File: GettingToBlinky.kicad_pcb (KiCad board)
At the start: 2 copper layers, 33 x 30.5 mm, 7 parts, among them U1 7555

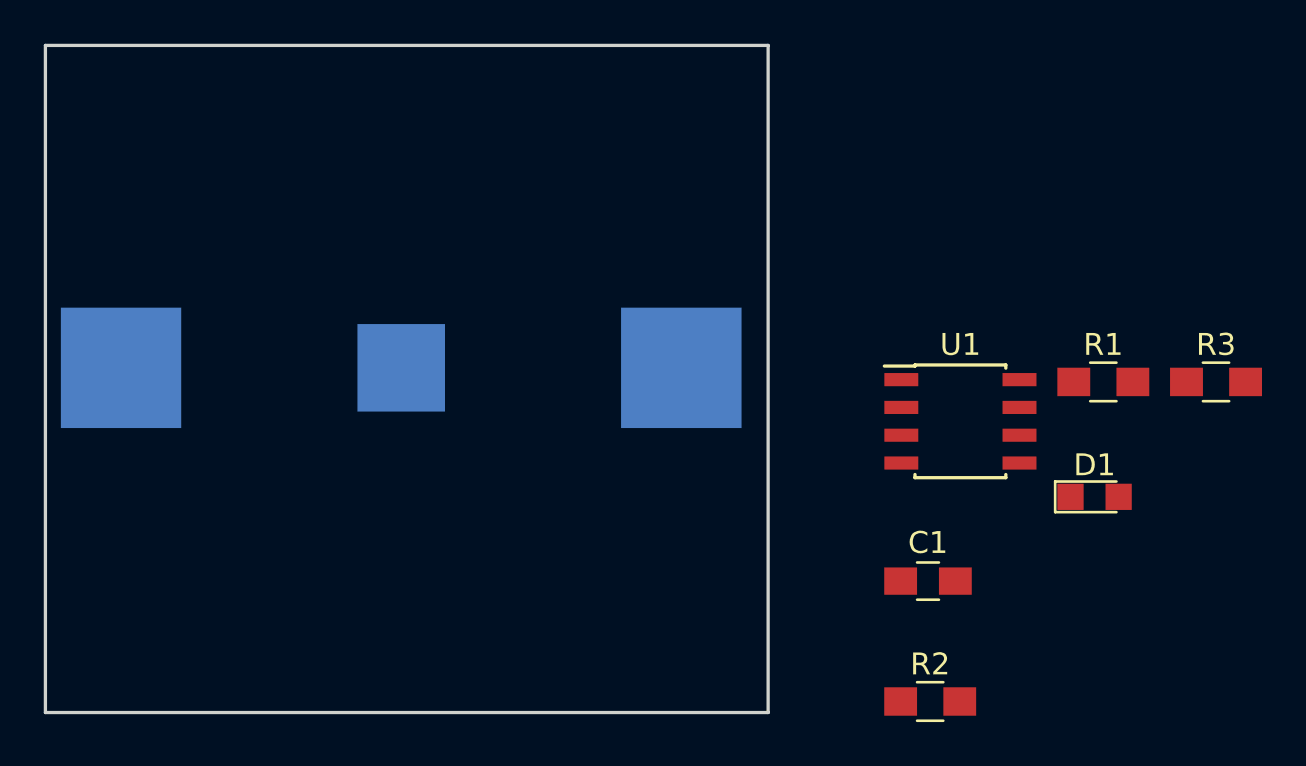
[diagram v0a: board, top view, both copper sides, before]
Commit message: finished connecting all the components with tracks and filled in the copper
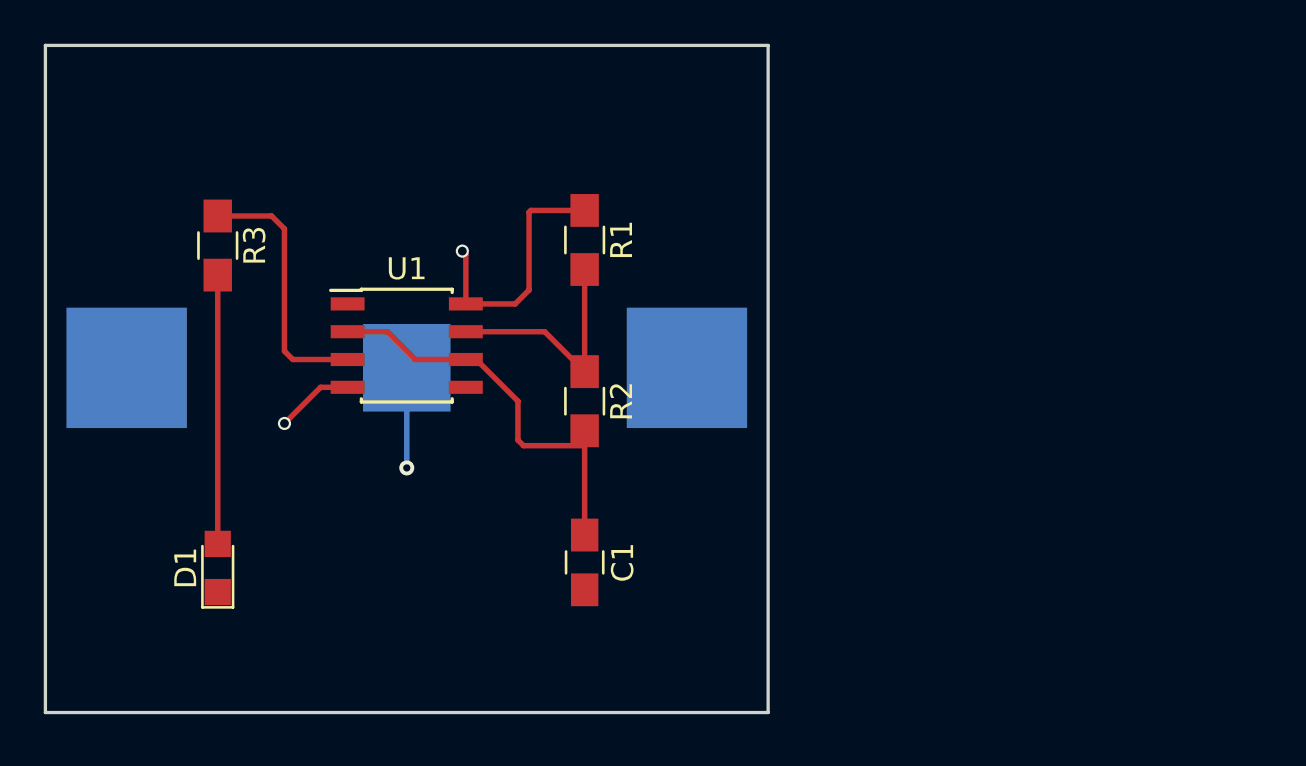
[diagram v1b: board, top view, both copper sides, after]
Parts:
- moved R3 46.0 mm to (96.8, 77.7), turned to 270 degrees
- moved D1 40.2 mm to (96.8, 92.5), turned to 90 degrees
- moved U1 25.5 mm to (105.4, 82.3)
- moved R1 24.6 mm to (113.5, 77.5), turned to 270 degrees
- moved R2 20.9 mm to (113.5, 84.8), turned to 270 degrees
- moved C1 15.7 mm to (113.5, 92.2), turned to 270 degrees
- moved BT1 0.25 mm to (105.4, 83.3)
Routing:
- net Net-(C1-Pad1): track 0.00 -> 19.5 mm
- net /VDD: track 0.00 -> 15.6 mm, vias 0 -> 2
- net Net-(D1-Pad2): track 0.00 -> 12.3 mm
- net Net-(R3-Pad1): track 0.00 -> 11.9 mm
- net Net-(R1-Pad2): track 0.00 -> 10.8 mm
- net GND: track 0.00 -> 4.57 mm, vias 0 -> 1
- added copper zone on B.Cu, net /VDD
- added copper zone on F.Cu, net GND
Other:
- net class Default: clearance 0.2 -> 0.254; trace_width 0.25 -> 0.254; via_dia 0.6 -> 0.6858; via_drill 0.4 -> 0.3302
- rule trace_clearance: 0.2 -> 0.254
- rule trace_min: 0.2 -> 0.1524
- rule via_min_drill: 0.3 -> 0.3302
- rule via_min_size: 0.4 -> 0.6858

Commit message: Updated silk layer to have text I wanted. Lastly ran the design rule checker to make sure all tracks are connected and design rule constraints are passing
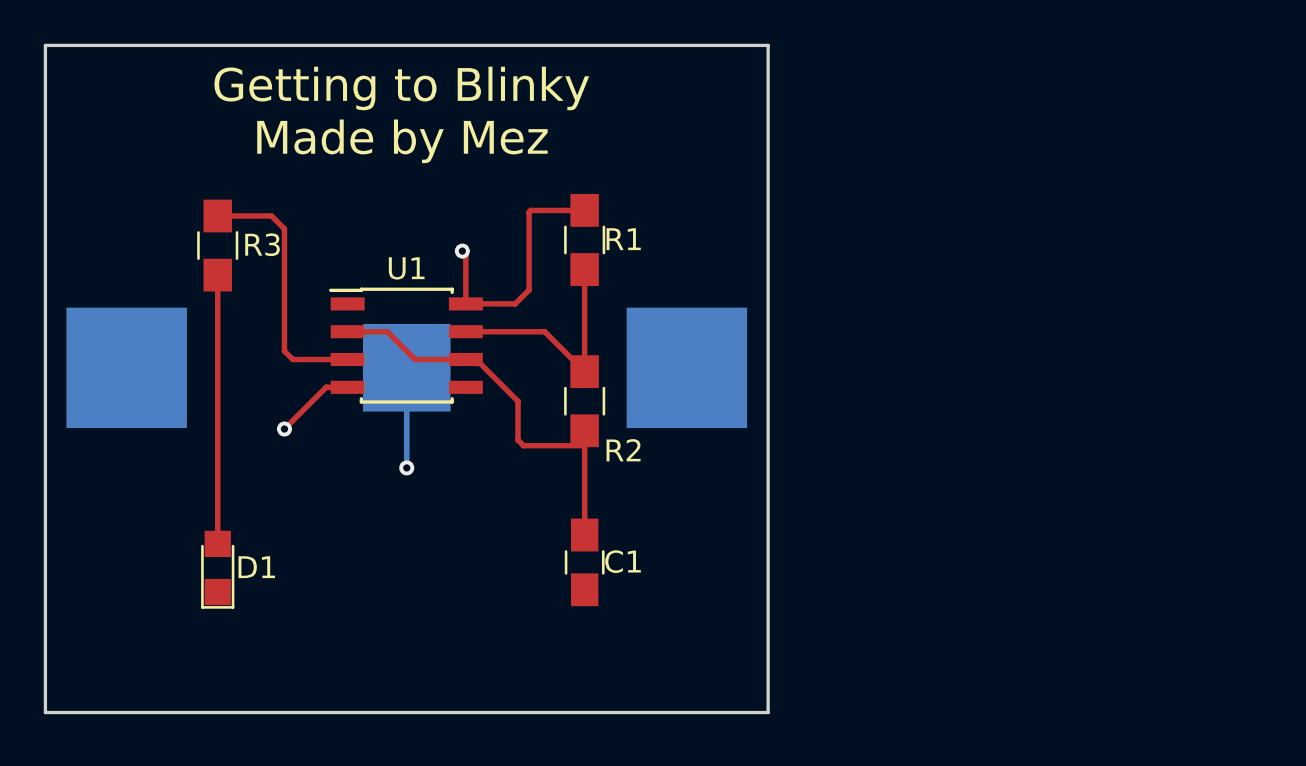
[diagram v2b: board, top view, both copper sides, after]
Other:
- board text added: "Getting to Blinky Made by Mez"
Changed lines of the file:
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@@
     (area 88.824999 68.504999 121.995001 99.135001)
     (thickness 1.6)
-    (drawings 4)
+    (drawings 5)
     (tracks 32)
     (zones 0)
@@
     (add_net "Net-(R3-Pad1)")
   )
+  (module GTB:S8211R (layer B.Cu)
+    (at 105.41 83.312)
+    (fp_text reference BT1 (at 14.478 12.192) (layer B.SilkS)
+      (effects (font (size 1 1) (thickness 0.15)) (justify mirror))
+    )
+    (fp_text value Battery (at -10.16 13.97) (layer B.Fab)
+      (effects (font (size 1 1) (thickness 0.15)) (justify mirror))
+    )
+    (fp_line (start -12.7 12.7) (end 12.7 12.7) (layer B.SilkS) (width 0.15))
+    (fp_line (start -12.7 -9.525) (end -12.7 12.7) (layer B.SilkS) (width 0.15))
+    (fp_line (start 0 -13.97) (end -12.7 -9.525) (layer B.SilkS) (width 0.15))
+    (fp_line (start 12.7 -10.16) (end 0 -13.97) (layer B.SilkS) (width 0.15))
+    (fp_line (start 12.7 12.7) (end 12.7 -10.16) (layer B.SilkS) (width 0.15))
+    (pad 1 smd rect (at 12.8 0) (size 5.5 5.5) (layers B.Cu B.Paste B.Mask)
+      (net 4 /VDD))
+    (pad 1 smd rect (at -12.8 0) (size 5.5 5.5) (layers B.Cu B.Paste B.Mask)
+      (net 4 /VDD))
+    (pad 2 smd rect (at 0 0) (size 4 4) (layers B.Cu B.Paste B.Mask)
+      (net 2 GND))
+  )
   (module Capacitors_SMD:C_0805_HandSoldering (layer F.Cu)
     (at 113.538 92.202 270)
@@
     (tags "capacitor 0805")
     (attr smd)
-    (fp_text reference C1 (at 0 -1.75 270) (layer F.SilkS)
+    (fp_text reference C1 (at 0 -1.778 360) (layer F.SilkS)
       (effects (font (size 1 1) (thickness 0.15)))
     )
@@
       (effects (font (size 1 1) (thickness 0.15)))
     )
-    (fp_text user %R (at 0 -1.75 270) (layer F.Fab)
+    (fp_text user "" (at 0 -1.75 270) (layer F.Fab)
       (effects (font (size 1 1) (thickness 0.15)))
     )
@@
     (tags "LED led 0805 SMD smd SMT smt smdled SMDLED smtled SMTLED")
     (attr smd)
-    (fp_text reference D1 (at 0 -1.45 90) (layer F.SilkS)
-      (effects (font (size 1 1) (thickness 0.15)))
-    )
-    (fp_text value LED (at 0 1.55 90) (layer F.Fab)
+    (fp_text reference D1 (at 0 1.778 180) (layer F.SilkS)
+      (effects (font (size 1 1) (thickness 0.15)))
+    )
+    (fp_text value LED (at 0 -1.524 90) (layer F.Fab)
       (effects (font (size 1 1) (thickness 0.15)))
     )
@@
     (tags "resistor 0805")
     (attr smd)
-    (fp_text reference R1 (at 0 -1.7 270) (layer F.SilkS)
+    (fp_text reference R1 (at 0 -1.778 360) (layer F.SilkS)
       (effects (font (size 1 1) (thickness 0.15)))
     )
@@
     (tags "resistor 0805")
     (attr smd)
-    (fp_text reference R2 (at 0 -1.7 270) (layer F.SilkS)
+    (fp_text reference R2 (at 2.286 -1.778 360) (layer F.SilkS)
       (effects (font (size 1 1) (thickness 0.15)))
     )
@@
     (tags "resistor 0805")
     (attr smd)
-    (fp_text reference R3 (at 0 -1.7 270) (layer F.SilkS)
+    (fp_text reference R3 (at 0 -2.032 360) (layer F.SilkS)
       (effects (font (size 1 1) (thickness 0.15)))
     )
@@
       (effects (font (size 1 1) (thickness 0.15)))
     )
-    (fp_text value 7555 (at 0 3.5) (layer F.Fab)
+    (fp_text value 7555 (at 0 -1.524) (layer F.Fab)
       (effects (font (size 1 1) (thickness 0.15)))
     )
@@
     )
   )
-  (module GTB:S8211R (layer B.Cu)
-    (at 105.41 83.312)
-    (fp_text reference BT1 (at 14.478 12.192) (layer B.SilkS)
-      (effects (font (size 1 1) (thickness 0.15)) (justify mirror))
-    )
-    (fp_text value Battery (at -10.16 13.97) (layer B.Fab)
-      (effects (font (size 1 1) (thickness 0.15)) (justify mirror))
-    )
-    (fp_line (start -12.7 12.7) (end 12.7 12.7) (layer B.SilkS) (width 0.15))
-    (fp_line (start -12.7 -9.525) (end -12.7 12.7) (layer B.SilkS) (width 0.15))
-    (fp_line (start 0 -13.97) (end -12.7 -9.525) (layer B.SilkS) (width 0.15))
-    (fp_line (start 12.7 -10.16) (end 0 -13.97) (layer B.SilkS) (width 0.15))
-    (fp_line (start 12.7 12.7) (end 12.7 -10.16) (layer B.SilkS) (width 0.15))
-    (pad 1 smd rect (at 12.8 0) (size 5.5 5.5) (layers B.Cu B.Paste B.Mask)
-      (net 4 /VDD))
-    (pad 1 smd rect (at -12.8 0) (size 5.5 5.5) (layers B.Cu B.Paste B.Mask)
-      (net 4 /VDD))
-    (pad 2 smd rect (at 0 0) (size 4 4) (layers B.Cu B.Paste B.Mask)
-      (net 2 GND))
+  (gr_text "Getting to Blinky\nMade by Mez" (at 105.156 71.628) (layer F.SilkS)
+    (effects (font (size 1.5 1.5) (thickness 0.3)))
   )
   (gr_line (start 121.92 99.06) (end 88.9 99.06) (angle 90) (layer Edge.Cuts) (width 0.15))
@@
   (gr_line (start 88.9 68.58) (end 121.92 68.58) (angle 90) (layer Edge.Cuts) (width 0.15))
   (gr_line (start 88.9 99.06) (end 88.9 68.58) (angle 90) (layer Edge.Cuts) (width 0.15))
-  (segment (start 113.538 86.186) (end 113.538 90.952) (width 0.254) (layer F.Cu) (net 1) (status C00000))
+  (segment (start 113.538 86.186) (end 113.538 90.952) (width 0.254) (layer F.Cu) (net 1))
   (segment (start 102.71 81.661) (end 104.521 81.661) (width 0.25) (layer F.Cu) (net 1))
   (segment (start 105.791 82.931) (end 108.11 82.931) (width 0.25) (layer F.Cu) (net 1))
@@
   (segment (start 110.744 86.868) (end 113.538 86.868) (width 0.25) (layer F.Cu) (net 1))
   (segment (start 113.538 86.868) (end 113.538 86.186) (width 0.25) (layer F.Cu) (net 1))
-  (segment (start 105.41 83.312) (end 105.41 87.884) (width 0.254) (layer B.Cu) (net 2) (status 400000))
+  (segment (start 105.41 83.312) (end 105.41 87.884) (width 0.254) (layer B.Cu) (net 2))
   (via (at 105.41 87.884) (size 0.6858) (drill 0.3302) (layers F.Cu B.Cu) (net 2))
   (segment (start 96.774 79.074) (end 96.774 91.356) (width 0.25) (layer F.Cu) (net 3))
-  (segment (start 102.71 84.201) (end 101.473 84.201) (width 0.25) (layer F.Cu) (net 4) (status 400000))
-  (via (at 99.822 85.852) (size 0.6) (drill 0.4) (layers F.Cu B.Cu) (net 4))
-  (segment (start 101.473 84.201) (end 99.822 85.852) (width 0.25) (layer F.Cu) (net 4))
-  (segment (start 108.11 80.391) (end 108.11 78.138) (width 0.25) (layer F.Cu) (net 4))
-  (via (at 107.95 77.978) (size 0.6) (drill 0.4) (layers F.Cu B.Cu) (net 4))
-  (segment (start 108.11 78.138) (end 107.95 77.978) (width 0.25) (layer F.Cu) (net 4))
-  (segment (start 108.11 80.391) (end 110.363 80.391) (width 0.25) (layer F.Cu) (net 4) (status 400000))
+  (segment (start 102.71 84.201) (end 101.727 84.201) (width 0.254) (layer F.Cu) (net 4))
+  (via (at 99.822 86.106) (size 0.6858) (drill 0.3302) (layers F.Cu B.Cu) (net 4))
+  (segment (start 101.727 84.201) (end 99.822 86.106) (width 0.254) (layer F.Cu) (net 4))
+  (segment (start 108.11 80.391) (end 108.11 78.138) (width 0.254) (layer F.Cu) (net 4))
+  (via (at 107.95 77.978) (size 0.6858) (drill 0.3302) (layers F.Cu B.Cu) (net 4))
+  (segment (start 108.11 78.138) (end 107.95 77.978) (width 0.254) (layer F.Cu) (net 4))
+  (segment (start 108.11 80.391) (end 110.363 80.391) (width 0.25) (layer F.Cu) (net 4))
   (segment (start 110.363 80.391) (end 110.998 79.756) (width 0.25) (layer F.Cu) (net 4))
   (segment (start 110.998 79.756) (end 110.998 76.2) (width 0.25) (layer F.Cu) (net 4))

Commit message: fixed bug that ran a track from pin 5 to GND. also added laser cutter format, so we can generate stencil for applying solder paste
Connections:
- U1 pad 5: GND -> Net-(U1-Pad5)
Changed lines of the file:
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@@
 (kicad_pcb (version 4) (host pcbnew 4.0.6)
   (general
-    (links 15)
+    (links 14)
     (no_connects 0)
     (area 88.824999 68.504999 121.995001 99.135001)
@@
     (zones 0)
     (modules 7)
-    (nets 7)
+    (nets 8)
   )
   (page A4)
@@
     (visible_elements FFFFFF7F)
     (pcbplotparams
-      (layerselection 0x00030_80000001)
+      (layerselection 0x00008_00000000)
       (usegerberextensions false)
       (excludeedgelayer true)
@@
       (psa4output false)
       (plotreference true)
-      (plotvalue true)
+      (plotvalue false)
       (plotinvisibletext false)
       (padsonsilk false)
       (subtractmaskfromsilk false)
-      (outputformat 1)
+      (outputformat 5)
       (mirror false)
-      (drillshape 1)
+      (drillshape 0)
       (scaleselection 1)
-      (outputdirectory ""))
+      (outputdirectory GERBERS/))
   )
   (net 0 "")
@@
   (net 5 "Net-(R1-Pad2)")
   (net 6 "Net-(R3-Pad1)")
+  (net 7 "Net-(U1-Pad5)")
   (net_class Default "This is the default net class."
     (clearance 0.254)
@@
     (add_net "Net-(R1-Pad2)")
     (add_net "Net-(R3-Pad1)")
+    (add_net "Net-(U1-Pad5)")
   )
   (module GTB:S8211R (layer B.Cu)
@@
       (net 4 /VDD))
     (pad 5 smd rect (at 2.7 1.905) (size 1.55 0.6) (layers F.Cu F.Paste F.Mask)
-      (net 2 GND))
+      (net 7 "Net-(U1-Pad5)"))
     (pad 6 smd rect (at 2.7 0.635) (size 1.55 0.6) (layers F.Cu F.Paste F.Mask)
       (net 1 "Net-(C1-Pad1)"))
